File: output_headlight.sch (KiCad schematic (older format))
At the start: 3 parts

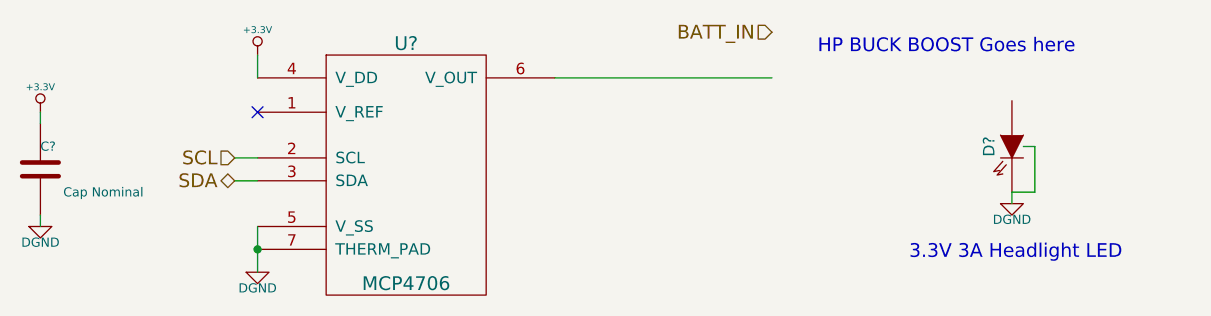
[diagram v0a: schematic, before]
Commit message: various fixes due to issues found in ERC
learned how to use invisible pins
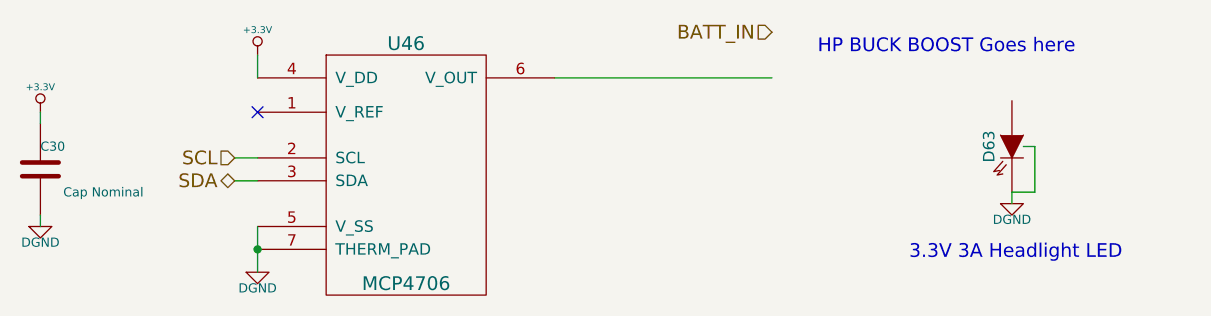
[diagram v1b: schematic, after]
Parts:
- gave numbers to parts that had none: 3
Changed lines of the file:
@@
 Sheet 14 18
 Title ""
-Date "18 dec 2013"
+Date "20 dec 2013"
 Rev ""
 Comp ""
@@
 $EndDescr
 $Comp
-L MCP4706 U?
+L MCP4706 U46
 U 1 1 52A38A2D
 P 2800 1150
-F 0 "U?" H 2800 1150 60  0000 C CNN
+F 0 "U46" H 2800 1150 60  0000 C CNN
 F 1 "MCP4706" H 2800 100 60  0000 C CNN
 F 2 "" H 2800 1150 60  0000 C CNN
@@
 $EndComp
 $Comp
-L XM-L2 D?
+L XM-L2 D63
 U 1 1 52A38BC7
 P 5450 1600
-F 0 "D?" H 5450 1500 50  0000 C CNN
+F 0 "D63" H 5450 1500 50  0000 C CNN
 F 1 "XM-L2" H 5450 1400 50  0001 C CNN
 F 2 "~" H 5450 1600 60  0000 C CNN
@@
 $EndComp
 $Comp
-L C C?
+L C C30
 U 1 1 52A39172
 P 1200 1700
-F 0 "C?" H 1200 1800 40  0000 L CNN
+F 0 "C30" H 1200 1800 40  0000 L CNN
 F 1 "Cap Nominal" H 1300 1600 40  0000 L CNN
 F 2 "~" H 1238 1550 30  0000 C CNN
@@
 $EndComp
 $Comp
-L +3.3V #PWR?
+L +3.3V #PWR099
 U 1 1 52A39178
 P 1200 1450
-F 0 "#PWR?" H 1200 1410 30  0001 C CNN
+F 0 "#PWR099" H 1200 1410 30  0001 C CNN
 F 1 "+3.3V" H 1200 1560 30  0000 C CNN
 F 2 "" H 1200 1450 60  0000 C CNN
@@
 $EndComp
 $Comp
-L DGND #PWR?
+L DGND #PWR0100
 U 1 1 52A3917E
 P 1200 1950
-F 0 "#PWR?" H 1200 1950 40  0001 C CNN
+F 0 "#PWR0100" H 1200 1950 40  0001 C CNN
 F 1 "DGND" H 1200 1880 40  0000 C CNN
 F 2 "" H 1200 1950 60  0000 C CNN
@@
 	1200 1900 1200 1950
 $Comp
-L DGND #PWR?
+L DGND #PWR0101
 U 1 1 52A39186
 P 5450 1850
-F 0 "#PWR?" H 5450 1850 40  0001 C CNN
+F 0 "#PWR0101" H 5450 1850 40  0001 C CNN
 F 1 "DGND" H 5450 1780 40  0000 C CNN
 F 2 "" H 5450 1850 60  0000 C CNN
@@
 BATT_IN
 $Comp
-L DGND #PWR?
+L DGND #PWR0102
 U 1 1 52A391D7
 P 2150 2150
-F 0 "#PWR?" H 2150 2150 40  0001 C CNN
+F 0 "#PWR0102" H 2150 2150 40  0001 C CNN
 F 1 "DGND" H 2150 2080 40  0000 C CNN
 F 2 "" H 2150 2150 60  0000 C CNN
@@
 	2150 1750 2050 1750
 $Comp
-L +3.3V #PWR?
+L +3.3V #PWR0103
 U 1 1 52A391FF
 P 2150 1200
-F 0 "#PWR?" H 2150 1160 30  0001 C CNN
+F 0 "#PWR0103" H 2150 1160 30  0001 C CNN
 F 1 "+3.3V" H 2150 1310 30  0000 C CNN
 F 2 "" H 2150 1200 60  0000 C CNN
